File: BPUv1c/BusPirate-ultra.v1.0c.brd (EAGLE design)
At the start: 100 x 50 mm, 172 parts, among them CON1 USB-C-12, IC1 SN74LVC1T45DBV, IC10 23LC1024, IC11 74HCT4051, IC12 MCP1824_ADJ, IC2 SN74LVC1T45DBV, IC3 SN74LVC1T45DBV, IC4 SN74LVC1T45DBV, IC5 SN74LVC1T45DBV, IC6 SN74LVC1T45DBV, IC7 SN74LVC1T45DBV, IC8 SN74LVC1T45DBV, IC9 23LC1024, J1 CON_HEADER_1X04, J2 CON_HEADER_1X10-RIGHT_ANGLED_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, J3 CON_MOLEX_MALE_SMT_SH_1.25, Q1 DMMT3906W, Q2 PMV65XP, U1 74LVC1G07DBV, U10 74HCT4066PW, U11 74HCT4066PW, U12 W25X40CL, U13 74LVC245A, U14 MCP6001, U15 MCP6001, U16 ICE40HX4K, U2 74LVC1G07DBV, U3 74LVC1G07DBV, U4 74LVC1G07DBV, U5 STM32F103ZX, U6 74LVC1G07DBV, U7 74LVC1G07DBV, U8 74LVC1G07DBV, U9 74LVC1G07DBV

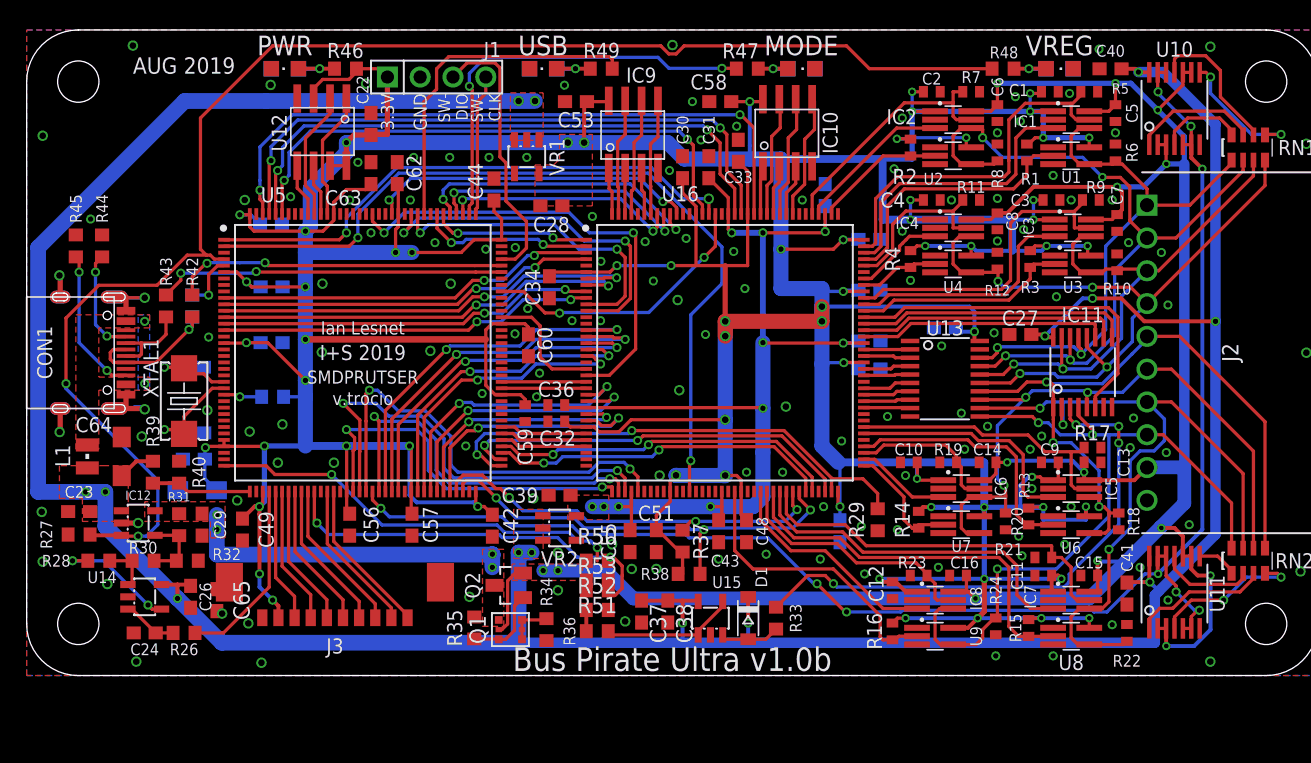
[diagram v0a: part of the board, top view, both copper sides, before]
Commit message: new BPUltra.v.1.0C revision removed some text labels renamed BPIO pin labels fix bom parts naming change back to original SC-70-5 and SC-70-6 footprints for 74LVC1G07DBV and SN74LVC1T45DBV added decoupling caps for open drain buffers broke RN3 to individual 10K R603 resistors Added 1uF 0603 cap to U14 connect OE (pin 80) and DIR (pin 81) of latch (245) to FPGA Change values of the following parts: R27 to 100K R32 to 10K R31 to 99.22K R30 to 77.96K R26 to 0R R36 to 0R R33 to 0R R34 to 65K R35 to 100K C24 to DNP C23 to 4.7uF C29 to 4.7uF D1 to 1N4148 Q2 to PMV65XP
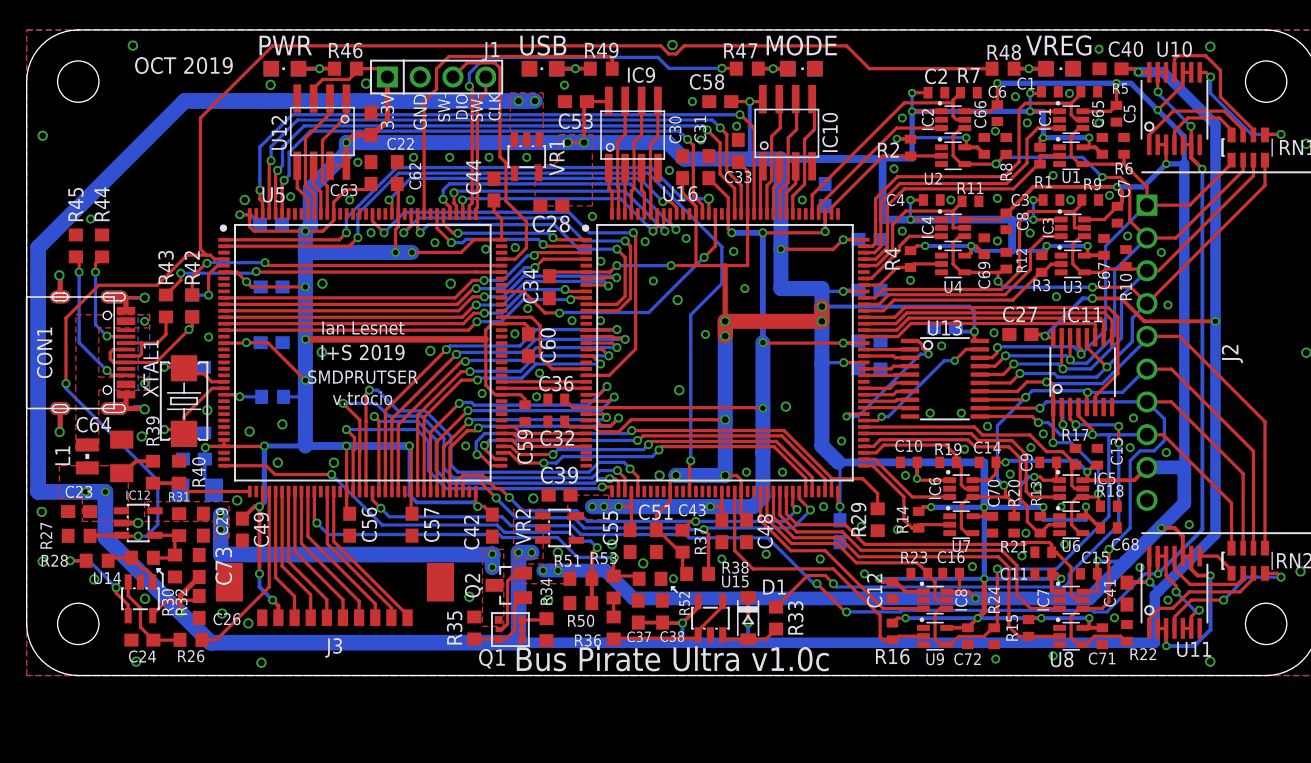
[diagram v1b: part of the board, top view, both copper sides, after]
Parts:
- added C66, C67, C68, C69, C70, C71, C72: 0.1uF, dp_devices.v6:C402
- added C73: 0.1uF, dp_devices.v6:C603
- C1, C5: device rcl:C0402 -> dp_devices.v6:C402
- C10, C11, C12, C13, C14, C15, C16, C2, C3, C4, C6, C7, C8, C9: device resistor:C0402 -> dp_devices.v6:C402
- C17, C18, C20, C21, C22, C24, C25, C26, C27, C30, C31, C33, C34, C35, C37, C38, C40, C41, C42, C43, C44, C45, C46, C47, C48, C49, C50, C51, C52, C53, C54, C55, C56, C57, C58, C60, C61, C62, C63: device rcl:C0603 -> dp_devices.v6:C603
- C19, C64: device rcl:SMC_A -> dp_devices.v6:SMC_A
- C28, C39: value 1uf -> 1uF; device rcl:C0603 -> dp_devices.v6:C603
- C65: value 1uF -> 0.1uF; device dp_devices.v6:C603 -> dp_devices.v6:C402
- IC1, IC2, IC3, IC4, IC5, IC6, IC7, IC8: device dp_devices.v6:SC-70-6_EXTENDED_PADS -> dp_devices.v6:SC-70-6
- R1, R10, R11, R12, R13, R14, R15, R16, R17, R18, R19, R2, R20, R21, R22, R23, R24, R3, R4, R5, R6, R7, R8, R9: device resistor:R0402 -> dp_devices.v6:R402
- R26, R29, R37, R38, R41, R42, R43, R44, R45: device rcl:R0603 -> dp_devices.v6:R603
- R33, R36, R39, R40: device resistor:R0603 -> dp_devices.v6:R603
- R46, R47, R48, R49: device dp_devices:R603 -> dp_devices.v6:R603
- U1, U2, U3, U4, U6, U7, U8, U9: device dp_devices.v6:SC-70-5_EXTENDED_PADS -> dp_devices.v6:SC-70-5
- XTAL1: device dp_devices:XTAL_4X6 -> dp_devices.v6:XTAL_4X6
- moved C65 77.1 mm to (83.3, 41.0)
- moved R52 4.75 mm to (48.3, 7.49)
- moved R50 3.51 mm to (42.9, 5.61), turned to 180 degrees
- moved U$4 2.29 mm to (60.7, 44.0)
- moved LOGO1 2.18 mm to (73.2, 44.5)
- moved R17 1.50 mm to (81.2, 16.9), turned to 270 degrees
- moved R18 1.39 mm to (83.8, 13.1), turned to 180 degrees
- moved R36 1.30 mm to (45.5, 3.68), turned to 90 degrees
- moved R53 1.30 mm to (45.5, 6.86), turned to 90 degrees
- moved R51 1.28 mm to (42.9, 7.49), turned to 0 degrees
- moved R13 1.11 mm to (78.5, 11.7)
- moved R1 1.05 mm to (78.5, 40.3)
- moved R32 1.05 mm to (11.5, 8.48), turned to 270 degrees
- moved C26 1.03 mm to (13.4, 5.31), turned to 90 degrees
- moved R3 0.97 mm to (78.6, 31.9)
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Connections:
- net 1V2: now also C31.1, C35.1, C39.2, C43.1, C54.1, C55.1; no longer C31.2, C35.2, C39.1, C43.2, C54.2, C55.2
- net 3V3: now also C1.2, C10.2, C11.2, C12.2, C17.1, C2.2, C21.1, C22.1, C25.1, C28.2, C3.2, C30.1, C33.1, C34.1, C4.2, C42.1, C44.1, C45.1, C46.1, C47.1, C48.1, C49.1, C50.1, C51.1, C52.1, C53.2, C56.1, C57.1, C58.2, C60.1, C61.2, C62.1, C63.1, C65.2, C66.2, C67.2, C68.2, C69.2, C70.2, C71.2, C72.2, C9.2; no longer C1.1, C10.1, C11.1, C12.1, C17.2, C2.1, C21.2, C22.2, C25.2, C28.1, C3.1, C30.2, C33.2, C34.2, C4.1, C42.2, C44.2, C45.2, C46.2, C47.2, C48.2, C49.2, C50.2, C51.2, C52.2, C53.1, C56.2, C57.2, C58.1, C60.2, C61.1, C62.2, C63.2, C9.1
- net ADC1: now also R52.1; no longer R52.2
- net GND: now also C1.1, C10.1, C11.1, C12.1, C13.2, C14.2, C15.2, C16.2, C17.2, C18.2, C2.1, C20.2, C21.2, C22.2, C24.1, C25.2, C26.1, C27.1, C28.1, C3.1, C30.2, C31.2, C33.2, C34.2, C35.2, C39.1, C4.1, C40.1, C41.1, C42.2, C43.2, C44.2, C45.2, C46.2, C47.2, C48.2, C49.2, C5.2, C50.2, C51.2, C52.2, C53.1, C54.2, C55.2, C56.2, C57.2, C58.1, C6.2, C60.2, C61.1, C62.2, C63.2, C65.1, C66.1, C67.1, C68.1, C69.1, C7.2, C70.1, C71.1, C72.1, C73.1, C8.2, C9.1, R50.2, R52.2; no longer C1.2, C10.2, C11.2, C12.2, C13.1, C14.1, C15.1, C16.1, C17.1, C18.1, C2.2, C20.1, C21.1, C22.1, C24.2, C25.1, C26.2, C27.2, C28.2, C3.2, C30.1, C31.1, C33.1, C34.1, C35.1, C39.2, C4.2, C40.2, C41.2, C42.1, C43.1, C44.1, C45.1, C46.1, C47.1, C48.1, C49.1, C5.1, C50.1, C51.1, C52.1, C53.2, C54.1, C55.1, C56.1, C57.1, C58.2, C6.1, C60.1, C61.2, C62.1, C63.1, C65.2, C7.1, C8.1, C9.2, R51.2, R53.1
- net MCU_ADC6: now also R50.1, R51.2; no longer R50.2, R51.1
- net N$21: now also R53.1; no longer R52.1
- net N$31: now also C24.2; no longer C24.1
- net N$8: now also C20.1; no longer C20.2
- net N$9: now also C18.1; no longer C18.2
- net VREF/VOUT: now also C13.1, C14.1, C15.1, C16.1, C5.1, C6.1, C7.1, C8.1, R51.1; no longer C13.2, C14.2, C15.2, C16.2, C5.2, C6.2, C7.2, C8.2, R50.1
- net VUSB: now also C26.2, C27.2, C40.2, C41.2, C73.2; no longer C26.1, C27.1, C40.1, C41.1, C65.1
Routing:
- net 3V3: track 573.9 -> 588.2 mm
- net LAT_DIR: track 0.00 -> 11.7 mm, vias 0 -> 2
- net LAT_OE: track 0.00 -> 11.3 mm, vias 0 -> 2
- net VREF/VOUT: track 187.0 -> 191.3 mm
- net VUSB: track 254.3 -> 258.5 mm
- net MCU_ADC6: track 32.6 -> 36.0 mm
- net N$31: track 4.26 -> 7.38 mm
- net BPIO1: track 58.7 -> 56.1 mm
- net BUFDIR4: track 22.1 -> 20.3 mm
- net N$15: track 9.62 -> 8.20 mm
- net BUFDIR1: track 19.5 -> 18.4 mm
- net BUFOD4: track 20.2 -> 21.2 mm
- net BPIO4: track 55.2 -> 54.3 mm
- net BUFDIR2: track 25.8 -> 24.9 mm
- net N$25: track 3.90 -> 4.58 mm
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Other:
- board text added: "BPIO0"
- board text added: "BPIO1"
- board text added: "BPIO2"
- board text added: "BPIO3"
- board text added: "BPIO4"
- board text added: "BPIO5"
- board text added: "BPIO6"
- board text added: "BPIO7"
- board text added: "Bus Pirate Ultra v1.0c"
- board text added: "OCT 2019"
- board text added: "VOUT"
- board text removed: "+5V"
- board text removed: "3V3"
- board text removed: "AUG 2019"
- board text removed: "AUX"
- board text removed: "Bus Pirate Ultra v1.0b"
- board text removed: "Fulfillment by"
- board text removed: "Seeed Studio"
- board text removed: "VPU"
- board text removed: "www.seeedstudio.com"

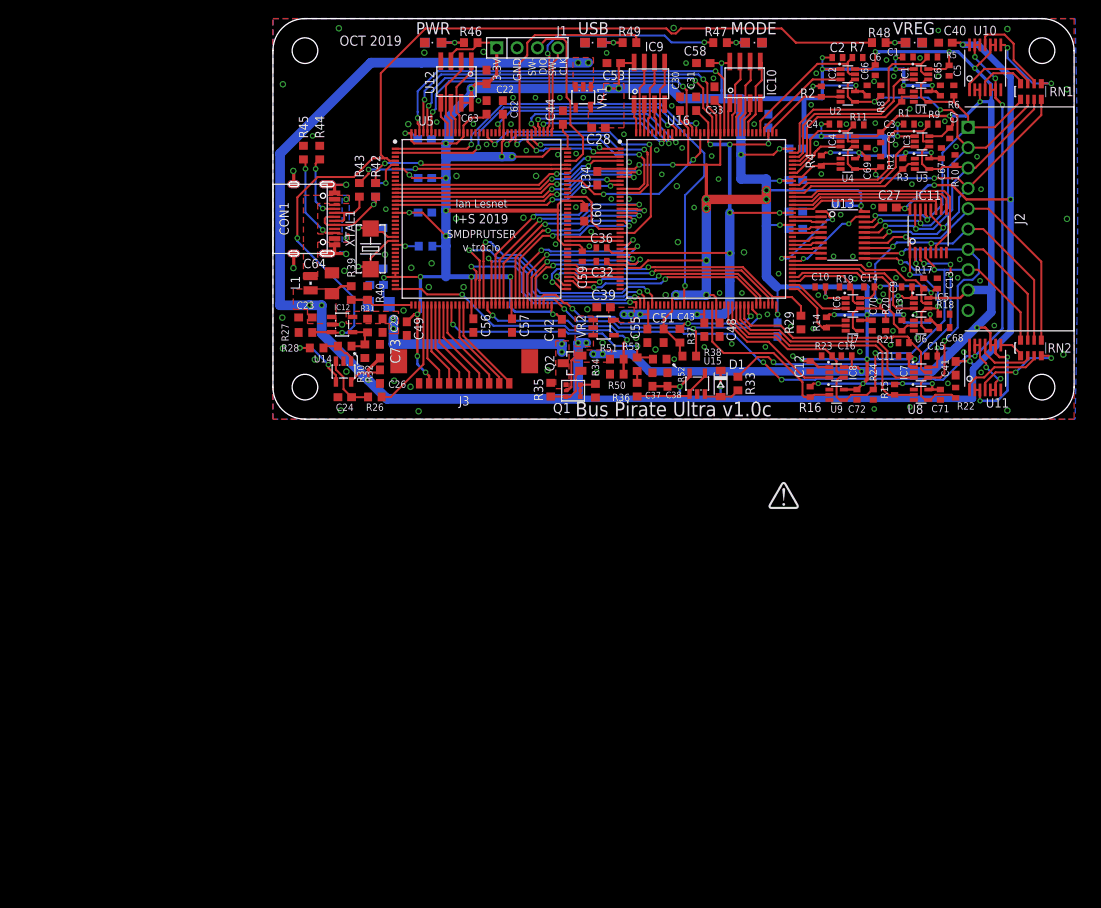
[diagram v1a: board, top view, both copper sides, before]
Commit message: re-number parts logically changed C302 to 1uF add 4.7uF input cap on VR1 add 4.7uF input cap on VR2 add RC filter 25R and 1.5nF on ADC MUX buffer
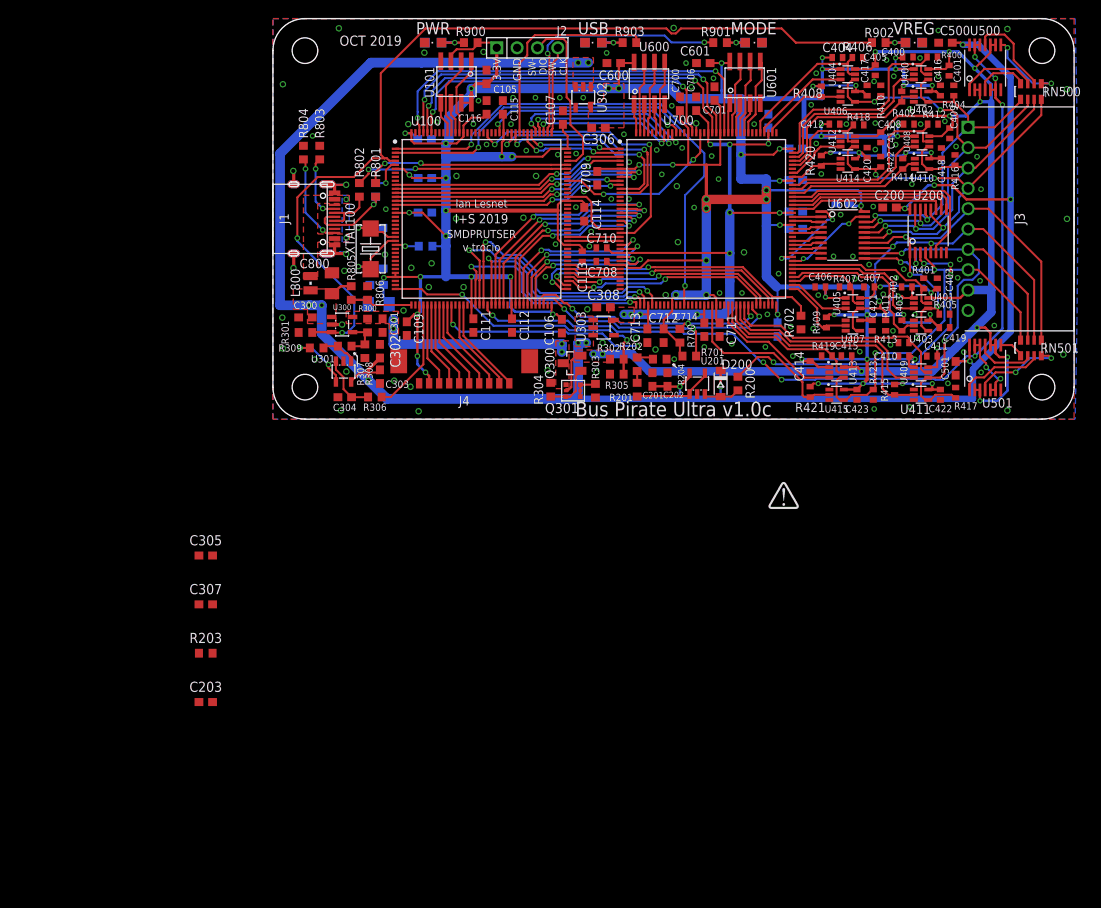
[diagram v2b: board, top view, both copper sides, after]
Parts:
- removed CON1: USB-C-12, usbc:C-31-M-12
- removed LED1, LED4, LED6, LED8: Optional YELLOW, dp_devices.v6:LED-805
- removed LED2, LED3, LED5, LED7: YELLOW, dp_devices.v6:LED-805
- removed R41: 1.5K, dp_devices.v6:R603
- removed R42: 22R, dp_devices.v6:R603
- added C203: 1.5nF, dp_devices.v6:C603
- added C305, C307: 4.7uF, dp_devices.v6:C603
- added J4: CON_MOLEX_MALE_SMT_SH_1.25, dp_devices.v6:MOLEX_533980771
- added LED900, LED901, LED902, LED903: YELLOW, dp_devices.v6:LED-805
- added LED904, LED905, LED906, LED907: Optional YELLOW, dp_devices.v6:LED-805
- added R203: 25R, dp_devices.v6:R603
- added R800: 1.5K, dp_devices.v6:R603
- added R801: 22R, dp_devices.v6:R603
- C302: value 0.1uF -> 1uF
- J1: value CON_HEADER_1X04 -> USB-C-12; device dp_devices.v6:M1X4 -> usbc:C-31-M-12
- J2: value CON_HEADER_1X10-RIGHT_ANGLED_PTH_SHROUDED -> CON_HEADER_1X04; device dp_devices.v6:M1X10_MALE_RIGHT_ANGLES_PTH_SHROUDED -> dp_devices.v6:M1X4
- J3: value CON_MOLEX_MALE_SMT_SH_1.25 -> CON_HEADER_1X10-RIGHT_ANGLED_PTH_SHROUDED; device dp_devices.v6:MOLEX_533980771 -> dp_devices.v6:M1X10_MALE_RIGHT_ANGLES_PTH_SHROUDED
- moved J3 71.9 mm to (93.2, 25.0), turned to 270 degrees
- moved J2 68.7 mm to (27.9, 46.4), turned to 0 degrees
- moved J1 31.6 mm to (4.69, 25.0), turned to 270 degrees
- renumbered C1 to C400, C10 to C406, C11 to C410, C12 to C414, C13 to C403, C14 to C407, C15 to C411, C16 to C415, C17 to C103, C18 to C100, C19 to C104, C2 to C404, C20 to C101, C21 to C102, C22 to C105, C23 to C300, C24 to C304, C25 to C715, C26 to C303, C27 to C200, C28 to C306, C29 to C301, C3 to C408, C30 to C700, C31 to C706, C32 to C708, C33 to C701, C34 to C709, C35 to C702, C36 to C710, C37 to C201, C38 to C202, C39 to C308, C4 to C412, C40 to C500, C41 to C501, C42 to C106, C43 to C714, C44 to C107, C45 to C707, C46 to C108, C47 to C703, C48 to C711, C49 to C109, C5 to C401, C50 to C704, C51 to C712, C52 to C110, C53 to C600, C54 to C705, C55 to C713, C56 to C111, C57 to C112, C58 to C601, C59 to C113, C6 to C405, C60 to C114, C61 to C602, C62 to C115, C63 to C116, C64 to C800, C65 to C416, C66 to C417, C67 to C418, C68 to C419, C69 to C420, C7 to C409, C70 to C421, C71 to C422, C72 to C423, C73 to C302, C8 to C413, C9 to C402, D1 to D200, IC1 to U400, IC10 to U601, IC11 to U200, IC12 to U300, IC2 to U404, IC3 to U408, IC4 to U412, IC5 to U401, IC6 to U405, IC7 to U409, IC8 to U413, IC9 to U600, L1 to L800, Q1 to Q301, Q2 to Q300, R1 to R402, R10 to R416, R11 to R418, R12 to R422, R13 to R403, R14 to R409, R15 to R415, R16 to R421, R17 to R401, R18 to R405, R19 to R407, R2 to R408, R20 to R411, R21 to R413, R22 to R417, R23 to R419, R24 to R423, R25 to R100, R26 to R306, R27 to R301, R28 to R309, R29 to R702, R3 to R414, R30 to R307, R31 to R300, R32 to R308, R33 to R200, R34 to R303, R35 to R304, R36 to R201, R37 to R700, R38 to R701, R39 to R805, R4 to R420, R40 to R806, R43 to R802, R44 to R803, R45 to R804, R46 to R900, R47 to R901, R48 to R902, R49 to R903, R5 to R400, R50 to R305, R51 to R302, R52 to R204, R53 to R202, R6 to R404, R7 to R406, R8 to R410, R9 to R412, RN1 to RN500, RN2 to RN501, U1 to U402, U10 to U500, U11 to U501, U12 to U101, U13 to U602, U14 to U301, U15 to U201, U16 to U700, U2 to U406, U3 to U410, U4 to U414, U5 to U100, U6 to U403, U7 to U407, U8 to U411, U9 to U415, VR1 to U302, VR2 to U303, XTAL1 to XTAL100
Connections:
- new net N$24: R202.2, R203.1, R204.1
- net 3V3: now also J2.1, J4.P9; no longer J1.1, J3.P9
- net ADC1: now also C203.1, R203.2; no longer R202.2, R204.1
- net BPIO0: now also J3.1; no longer J2.1
- net BPIO1: now also J3.2; no longer J2.2
- net BPIO2: now also J3.3; no longer J2.3
- net BPIO3: now also J3.4; no longer J2.4
- net BPIO4: now also J3.5; no longer J2.5
- net BPIO5: now also J3.6; no longer J2.6
- net BPIO6: now also J3.7; no longer J2.7
- net BPIO7: now also J3.8; no longer J2.8
- net D+: now also J1.DP1, J1.DP2, R800.1, R801.2; no longer CON1.DP1, CON1.DP2, R41.1, R42.2
- net D-: now also J1.DN1, J1.DN2; no longer CON1.DN1, CON1.DN2
- net DISPLAY_AUX1: now also J4.P5; no longer J3.P5
- net DISPLAY_AUX2: now also J4.P4; no longer J3.P4
- net DISPLAY_CS: now also J4.P1; no longer J3.P1
- net DISPLAY_D/P: now also J4.P2; no longer J3.P2
- net DISPLAY_PWM: now also J4.P3; no longer J3.P3
- net DISPLAY_SPI_CLOCK: now also J4.P8; no longer J3.P8
- net DISPLAY_SPI_MISO: now also J4.P7; no longer J3.P7
- net DISPLAY_SPI_MOSI: now also J4.P6; no longer J3.P6
- net GND: now also C203.2, C305.1, C307.1, J1.GND@1, J1.GND@2, J1.P$1, J1.P$2, J1.P$3, J1.P$4, J1.P$5, J1.P$6, J1.P$7, J1.P$8, J2.2, J3.10, J4.P10, LED900.C, LED901.C, LED902.C, LED903.C, LED904.C, LED905.C, LED906.C, LED907.C; no longer CON1.GND@1, CON1.GND@2, CON1.P$1, CON1.P$2, CON1.P$3, CON1.P$4, CON1.P$5, CON1.P$6, CON1.P$7, CON1.P$8, J1.2, J2.10, J3.P10, LED1.C, LED2.C, LED3.C, LED4.C, LED5.C, LED6.C, LED7.C, LED8.C
- net N$1: now also J1.VBUS@1, J1.VBUS@2; no longer CON1.VBUS@1, CON1.VBUS@2
- net N$13: now also LED903.A, LED907.A; no longer LED7.A, LED8.A
- net N$14: now also J1.CC1; no longer CON1.CC1
- net N$18: now also LED902.A, LED906.A; no longer LED5.A, LED6.A
- net N$20: now also J1.CC2; no longer CON1.CC2
- net N$6: now also LED901.A, LED905.A; no longer LED3.A, LED4.A
- net N$7: now also LED900.A, LED904.A; no longer LED1.A, LED2.A
- net SWCLK: now also J2.4; no longer J1.4
- net SWDIO: now also J2.3; no longer J1.3
- net USB_D+: now also R801.1; no longer R42.1
- net USB_DET: now also R800.2; no longer R41.2
- net VREF/VOUT: now also J3.9; no longer J2.9
- net VUSB: now also C305.2, C307.2
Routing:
- net ADC1: track 30.3 -> 26.7 mm
- net N$24: track 0.00 -> 2.18 mm

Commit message: added ADC ADS7041 and wired to FPGA pin 45, 47 and 48 changed 3.3V regulator to bigger MCP1700 changed mux to 16-bit version 74HCT4067, added one new address line S3 to FPGA (not connected yet) connected 1.2V VREG output to MCU ADC pin 35 PA1 changed VUSB voltage divider resistors R805 and R806 to 50K
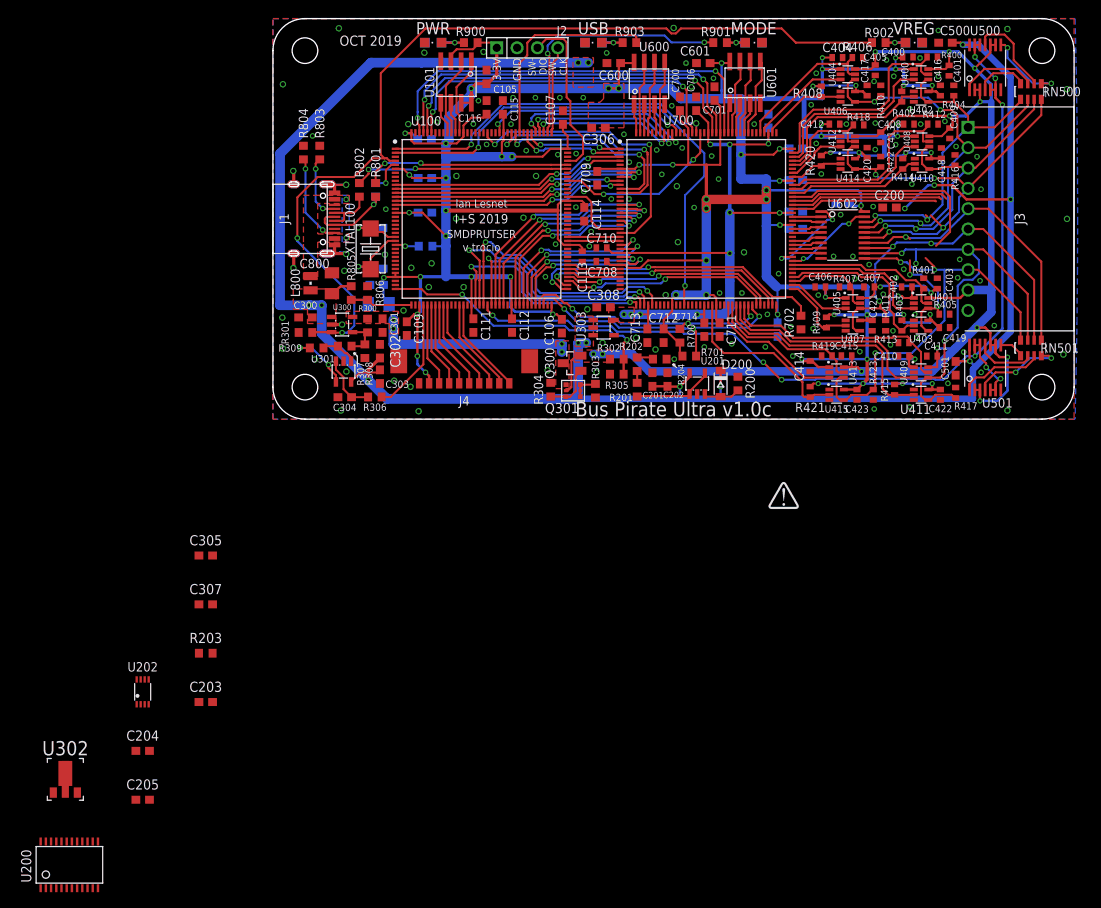
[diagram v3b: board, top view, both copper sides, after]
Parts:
- added C204, C205: 1uF, dp_devices.v6:C603
- added U202: ADS7041, dp_devices.v6:VSSOP-8_DCU_PDSO_G8
- R805, R806: value 10K -> 50K
- U200: value 74HCT4051 -> 74HCT4067; device dp_devices.v6:TSSOP-16 -> dp_devices.v6:TSSOP-24
- U302: value MCP1801T-3302I/OT -> MCP1700; device dp_devices:SOT-23-5@1 -> dp_devices.v6:SOT-89
- moved U200 133.2 mm to (-25.4, -55.6)
- moved U302 106.9 mm to (-25.9, -45.0), turned to 0 degrees
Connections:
- removed net ADC1: C203.1, R203.2, U100.47
- removed net N$10: U100.35
- removed net N$61: R200.1, U200.3
- new net ADC_CLOCK: U202.2, U700.47
- new net ADC_CS: U202.4, U700.45
- new net ADC_DATA: U202.3, U700.48
- new net ADC_MUX_S3: U200.13
- new net N$46: C203.1, R203.2, U202.6
- new net N$47: R200.1, U200.1
- net 1V2: now also U100.35
- net 3V3: now also U302.3; no longer U302.5
- net ADC_MUX_EN: now also U200.15; no longer U200.6
- net ADC_MUX_S0: now also U200.10; no longer U200.11
- net ADC_MUX_S1: now also U200.11; no longer U200.10
- net ADC_MUX_S2: now also U200.14; no longer U200.9
- net BPIO0: now also U200.9; no longer U200.13
- net BPIO1: now also U200.8; no longer U200.14
- net BPIO2: now also U200.7; no longer U200.15
- net BPIO3: now also U200.6; no longer U200.12
- net BPIO4: now also U200.5; no longer U200.1
- net BPIO5: now also U200.4; no longer U200.5
- net BPIO6: now also U200.3; no longer U200.2
- net BPIO7: now also U200.2; no longer U200.4
- net GND: now also C204.2, C205.2, U200.12, U202.5, U202.8, U302.1; no longer U200.7, U200.8, U302.2
- net VREF/VOUT: now also U200.23
- net VUSB: now also C204.1, C205.1, U200.24, U202.1, U202.7, U302.2; no longer U200.16, U302.1, U302.3
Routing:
- net N$61: track 42.8 -> 0.00 mm, vias 4 -> 0
- net ADC1: track 26.7 -> 0.00 mm, vias 2 -> 0
- net BPIO4: track 54.3 -> 51.7 mm
- net BPIO2: track 42.7 -> 40.4 mm
- net BPIO1: track 56.1 -> 54.4 mm
- net VUSB: track 258.5 -> 257.0 mm
- net ADC_MUX_S2: track 21.1 -> 19.8 mm
- net BPIO6: track 60.3 -> 59.1 mm
- net ADC_MUX_S1: track 20.3 -> 19.1 mm
- net BPIO5: track 50.9 -> 49.8 mm
- net ADC_MUX_S0: track 19.4 -> 18.4 mm
- net ADC_MUX_EN: track 28.0 -> 27.1 mm
- net BPIO3: track 54.8 -> 54.1 mm
- net BPIO0: track 43.6 -> 42.9 mm
- net BPIO7: track 58.2 -> 57.5 mm
